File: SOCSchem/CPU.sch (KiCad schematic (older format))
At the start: 28 parts

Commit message: Various improvments and fixes
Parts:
- removed U?: IRAM, symbol SOC:IRAM
- added U?: LOAD_UPPER, symbol SOC:LOAD_UPPER
- added U?: 2-1Mux, symbol SOC:2-1Mux
- added U?: IBUS, symbol SOC:IBUS
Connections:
- net labels added: DBusRe_E, ExeResSel_E, ExeRes_M, ExeSignNeg_M, ExeZero_M, IBusOZero_D, IBusRdEn_D, IBus_WaitReq_D, LoadUpperOp_E
- net labels removed: DBusRe_D, DBusWe_D, IRamOZero_D, IRamRdEn_D
- wire segments 127 -> 136

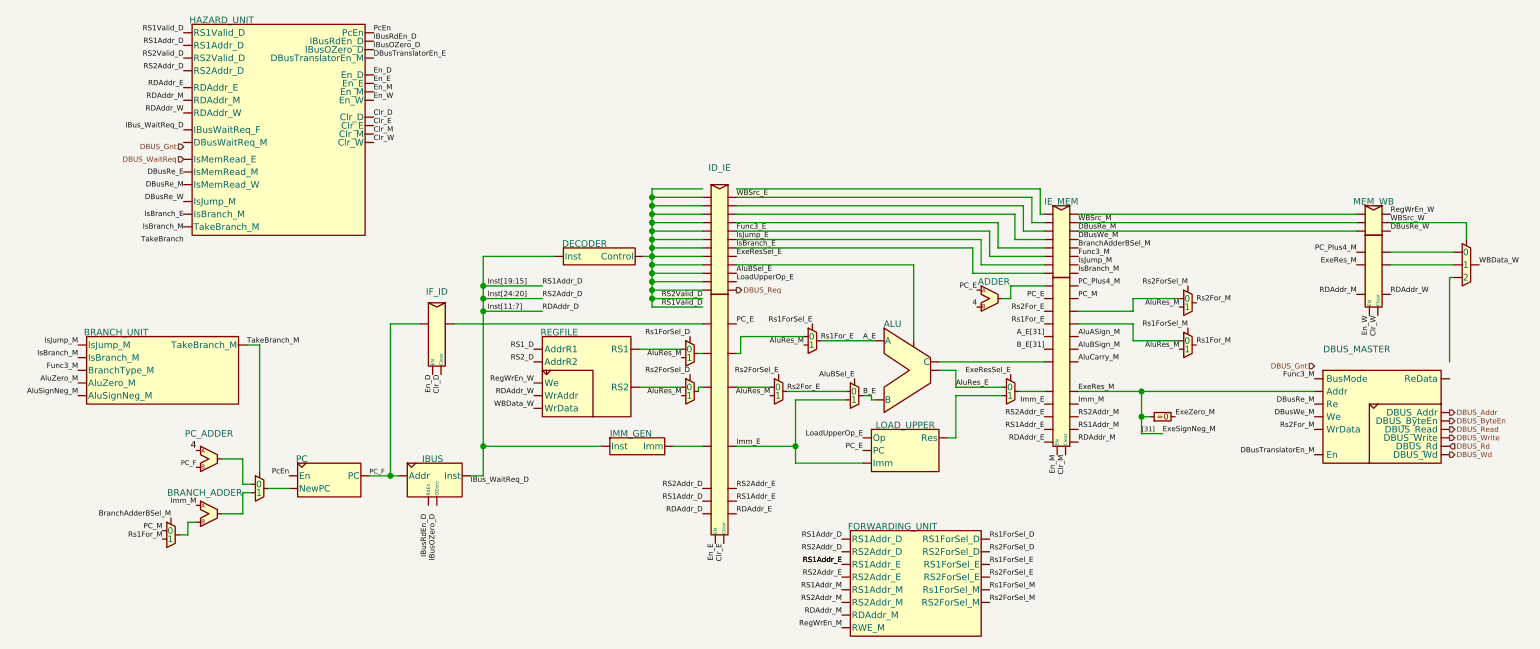
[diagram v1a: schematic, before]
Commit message: Integrated the interconnect into the SOC, in progress
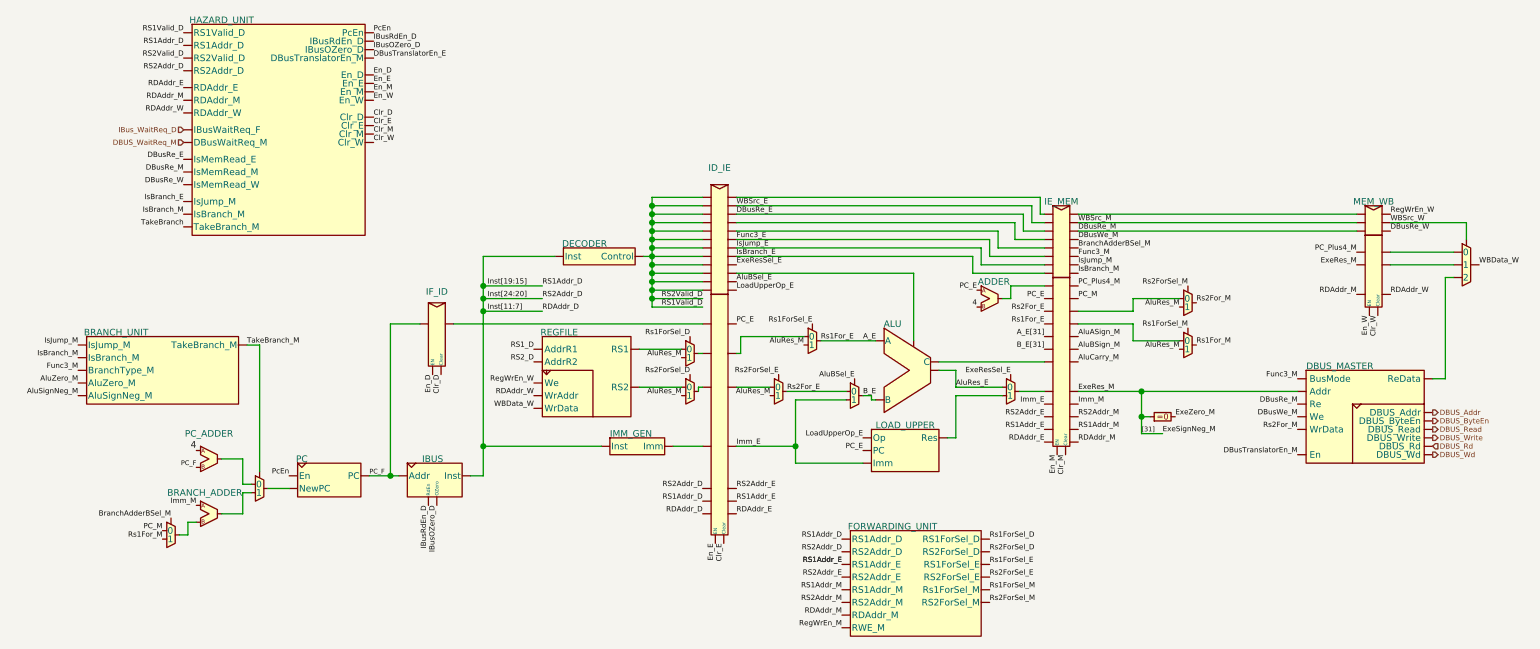
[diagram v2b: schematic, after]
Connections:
- net DBUS_Req is gone; now on net WBSrc_E: U?.~
- net DBUS_WaitReq is gone; now on net TakeBranch: U?.~ (TakeBranch_M)
- net DBusRe_E: now also U?.~, U?.~, U?.~ (TakeBranch_M)
- net DBusRe_M: now also U?.~ (TakeBranch_M)
- net IBusOZero_D: now also U?.~ (RdEn)
- net IBusRdEn_D: now also U?.~ (RdEn)
- net IsBranch_E: now also U?.~ (TakeBranch_M)
- net IsBranch_M: now also U?.~ (TakeBranch_M)
- new net: U?.~, U?.~ (x20)
- new net: U?.~, U?.~ (Res)
- new net: U?.~, U?.~ (WrData) (x3)
- new net: U?.~, U?.~ (Inst)
- new net: U?.~, U?.~ (PC)
- new net DBUS_WaitReq_M: U?.~ (TakeBranch_M)
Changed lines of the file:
@@
 EESchema Schematic File Version 4
-LIBS:SOCSchem-cache
 EELAYER 30 0
 EELAYER END
 $Descr A4 11693 8268
 encoding utf-8
-Sheet 2 2
+Sheet 1 1
 Title ""
 Date ""
@@
 Text Label 5475 4225 0    31   ~ 0
 RDAddr_E
-Text Label 5475 2350 0    31   ~ 0
+Text Label 5475 2400 0    31   ~ 0
 WBSrc_E
 Wire Wire Line
@@
 Text Label 5475 3100 0    31   ~ 0
 PC_E
-Text Label 8900 3650 2    31   ~ 0
+Text Label 8800 3650 2    31   ~ 0
 DBusWe_M
-Text Label 8900 3575 2    31   ~ 0
+Text Label 8800 3575 2    31   ~ 0
 DBusRe_M
-Text Label 8900 3425 2    31   ~ 0
+Text Label 8800 3425 2    31   ~ 0
 Func3_M
 Text Label 7300 3575 2    31   ~ 0
@@
 L SOC:DBUS_MASTER U?
 U 1 1 5EBA31C6
-P 9150 3450
+P 9050 3450
 AR Path="/5EBA31C6" Ref="U?"  Part="1"
 AR Path="/5EB97B98/5EBA31C6" Ref="U?"  Part="1"
-F 0 "U?" H 9000 3750 50  0001 C CNN
-F 1 "DBUS_MASTER" H 9150 3650 39  0000 C CNN
-F 2 "" H 9050 3700 50  0001 C CNN
-F 3 "" H 9050 3700 50  0001 C CNN
-	1    9150 3450
+F 0 "U?" H 8900 3750 50  0001 C CNN
+F 1 "DBUS_MASTER" H 9050 3550 39  0000 C CNN
+F 2 "" H 8950 3700 50  0001 C CNN
+F 3 "" H 8950 3700 50  0001 C CNN
+	1    9050 3450
 	1    0    0    -1
 $EndComp
@@
 	1    0    0    -1
 $EndComp
-Text HLabel 9700 3625 2    31   Output ~ 0
+Text HLabel 9600 3625 2    31   Output ~ 0
 DBUS_Addr
-Text HLabel 9700 3675 2    31   Output ~ 0
+Text HLabel 9600 3675 2    31   Output ~ 0
 DBUS_ByteEn
-Text HLabel 9700 3725 2    31   Output ~ 0
+Text HLabel 9600 3725 2    31   Output ~ 0
 DBUS_Read
-Text HLabel 9700 3775 2    31   Output ~ 0
+Text HLabel 9600 3775 2    31   Output ~ 0
 DBUS_Write
-Text HLabel 9700 3825 2    31   Input ~ 0
+Text HLabel 9600 3825 2    31   Input ~ 0
 DBUS_Rd
-Text HLabel 9700 3875 2    31   Output ~ 0
+Text HLabel 9600 3875 2    31   Output ~ 0
 DBUS_Wd
-Text HLabel 5475 2900 2    31   Output ~ 0
-DBUS_Req
-Text Label 8900 3875 2    31   ~ 0
+Text Label 8800 3875 2    31   ~ 0
 DBusTranslatorEn_M
 Wire Wire Line
@@
 Text Label 7500 2700 0    31   ~ 0
 Func3_M
-Text HLabel 8900 3350 0    31   Input ~ 0
-DBUS_Gnt
-Text Label 5475 2550 0    31   ~ 0
+Text Label 5475 2600 0    31   ~ 0
 Func3_E
 $Comp
@@
 Text Label 2200 1700 2    31   ~ 0
 RDAddr_E
-Text Label 2200 2550 2    31   ~ 0
+Text Label 2200 2450 2    31   ~ 0
 IsBranch_M
 $Comp
@@
 Text Label 2575 3225 0    31   ~ 0
 TakeBranch_M
-Text Label 2200 2625 2    31   ~ 0
+Text Label 2200 2525 2    31   ~ 0
 TakeBranch
 Text Label 3675 3400 3    31   ~ 0
@@
 Text Label 1575 3525 2    31   ~ 0
 AluSignNeg_M
-Text HLabel 2200 2050 0    31   Input ~ 0
-DBUS_Gnt
-Text HLabel 2200 2125 0    31   Input ~ 0
-DBUS_WaitReq
+Text HLabel 2200 2025 0    31   Input ~ 0
+DBUS_WaitReq_M
 Text Label 3325 1525 0    31   ~ 0
 DBusTranslatorEn_E
@@
 Wire Wire Line
 	5475 3275 5500 3275
-Text Label 5475 2650 0    31   ~ 0
+Text Label 5475 2700 0    31   ~ 0
 IsBranch_E
-Text Label 2200 2225 2    31   ~ 0
+Text Label 2200 2125 2    31   ~ 0
 DBusRe_E
 Wire Wire Line
@@
 Text Label 7500 2750 0    31   ~ 0
 IsJump_M
-Text Label 5475 2600 0    31   ~ 0
+Text Label 5475 2650 0    31   ~ 0
 IsJump_E
-Text Label 2200 2475 2    31   ~ 0
+Text Label 2200 2375 2    31   ~ 0
 IsBranch_E
 Text Label 1575 3225 2    31   ~ 0
@@
 	9350 2750 9725 2750
 Wire Wire Line
-	9700 2825 9725 2825
+	9675 2825 9725 2825
 Wire Wire Line
 	9350 2500 9800 2500
@@
 Text Label 8200 2975 0    31   ~ 0
 Rs2For_M
-Text Label 8900 3725 2    31   ~ 0
+Text Label 8800 3725 2    31   ~ 0
 Rs2For_M
 Text Label 6975 4750 0    31   ~ 0
@@
 $EndComp
 Wire Wire Line
-	5475 2650 6875 2650
-Wire Wire Line
-	5475 2600 6925 2600
-Wire Wire Line
-	5475 2550 6975 2550
-Wire Wire Line
-	5475 2500 7025 2500
-Wire Wire Line
-	5475 2450 7125 2450
-Wire Wire Line
-	5475 2400 7175 2400
-Wire Wire Line
-	5475 2350 7225 2350
+	5475 2700 6875 2700
+Wire Wire Line
+	5475 2650 6925 2650
+Wire Wire Line
+	5475 2600 6975 2600
+Wire Wire Line
+	5475 2550 7025 2550
+Wire Wire Line
+	5475 2500 7125 2500
+Wire Wire Line
+	5475 2450 7175 2450
+Wire Wire Line
+	5475 2400 7225 2400
 $Comp
 L SOC:2-1Mux U?
@@
 	6775 3525 7050 3525
 Wire Wire Line
-	7500 3500 7875 3500
-Wire Wire Line
 	6675 3375 6775 3375
 Wire Wire Line
@@
 	4975 2350 4975 2400
 Connection ~ 4975 2400
-Wire Wire Line
-	5275 2300 4975 2300
-Wire Wire Line
-	4975 2300 4975 2350
-Connection ~ 4975 2350
-Wire Wire Line
-	6875 2650 6875 2800
-Wire Wire Line
-	6925 2600 6925 2750
-Wire Wire Line
-	6975 2550 6975 2700
-Wire Wire Line
-	7225 2350 7225 2500
-Wire Wire Line
-	7175 2400 7175 2550
-Wire Wire Line
-	7125 2450 7125 2600
-Wire Wire Line
-	7025 2500 7025 2650
 Text Label 2200 1850 2    31   ~ 0
 RDAddr_W
-Text Label 2200 2300 2    31   ~ 0
+Text Label 2200 2200 2    31   ~ 0
 DBusRe_M
-Text Label 2200 2375 2    31   ~ 0
+Text Label 2200 2275 2    31   ~ 0
 DBusRe_W
-Wire Wire Line
-	6525 2750 5475 2750
-Text Label 5475 2800 0    31   ~ 0
+Text Label 5475 2850 0    31   ~ 0
 AluBSel_E
-Wire Wire Line
-	6525 2750 6525 3200
-Text Label 5475 2850 0    31   ~ 0
+Text Label 5475 2900 0    31   ~ 0
 LoadUpperOp_E
 Text Label 6225 3775 2    31   ~ 0
 LoadUpperOp_E
-Text Label 5475 2700 0    31   ~ 0
+Text Label 5475 2750 0    31   ~ 0
 ExeResSel_E
 Text Label 7100 3400 2    31   ~ 0
 ExeResSel_E
-Wire Wire Line
-	9700 2825 9700 3325
-Wire Wire Line
-	5475 2300 7275 2300
-Wire Wire Line
-	7275 2300 7275 2450
 Text Label 7500 3500 0    31   ~ 0
 ExeRes_M
@@
 Wire Wire Line
 	9800 2500 9800 2600
-Connection ~ 7875 3500
-Wire Wire Line
-	7875 3500 8900 3500
 $Comp
 L SOC:IBUS U?
@@
 	1    0    0    -1
 $EndComp
-Text Label 3900 4050 0    31   ~ 0
-IBus_WaitReq_D
-Text Label 3650 4225 3    31   ~ 0
+Text Label 3650 4175 3    31   ~ 0
 IBusRdEn_D
-Text Label 3700 4225 3    31   ~ 0
+Text Label 3700 4175 3    31   ~ 0
 IBusOZero_D
-Text Label 2200 1950 2    31   ~ 0
+Wire Wire Line
+	6875 2700 6875 2800
+Wire Wire Line
+	6925 2650 6925 2750
+Wire Wire Line
+	6975 2600 6975 2700
+Wire Wire Line
+	7025 2550 7025 2650
+Wire Wire Line
+	7125 2500 7125 2600
+Wire Wire Line
+	7175 2450 7175 2550
+Wire Wire Line
+	7225 2400 7225 2500
+Wire Wire Line
+	7275 2350 7275 2450
+Wire Wire Line
+	5475 2350 7275 2350
+Wire Wire Line
+	5475 2800 6525 2800
+Wire Wire Line
+	6525 2800 6525 3200
+Wire Wire Line
+	9675 2825 9675 3425
+Wire Wire Line
+	7500 3500 7875 3500
+Wire Wire Line
+	9600 3425 9675 3425
+Wire Wire Line
+	8800 3500 7875 3500
+Connection ~ 7875 3500
+Text Label 5475 2450 0    31   ~ 0
+DBusRe_E
+Text HLabel 2200 1950 0    31   Input ~ 0
 IBus_WaitReq_D
 $EndSCHEMATC
